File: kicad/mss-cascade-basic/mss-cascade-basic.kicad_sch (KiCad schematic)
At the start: 93 parts, among them J1 Screw_Terminal_01x02, J10 Screw_Terminal_01x02, J2 SM04B-SRSS, J3 SM04B-SRSS, J4 SM04B-SRSS, J5 8P8C, J6 8P8C, J7 AVR-ISP, J8 Screw_Terminal_01x02, J9 Screw_Terminal_01x02, U1 AP7381-50Y, U2 ATtiny861A-S, U3 74HC4049, U4 AP3012

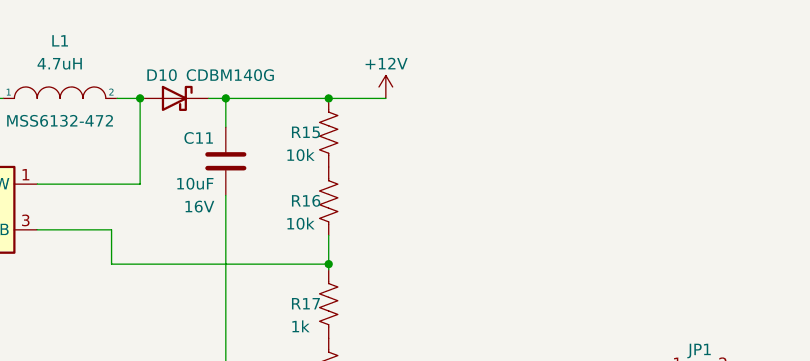
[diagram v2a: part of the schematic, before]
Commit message: Add test point for 12V, move connectors to align
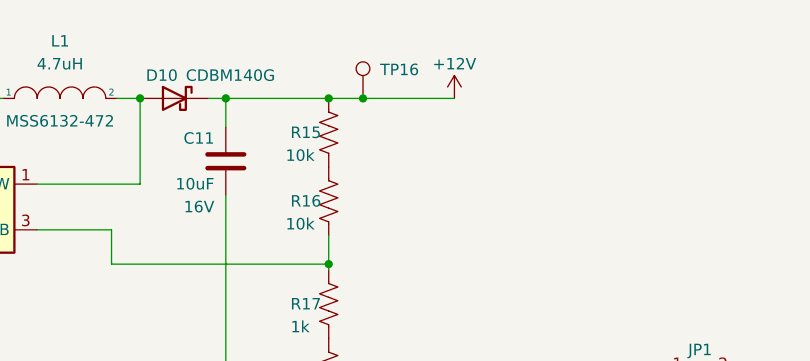
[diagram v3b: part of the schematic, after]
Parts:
- added TP16: TestPoint, TestPoint:TestPoint_Pad_D2.0mm, symbol Connector:TestPoint
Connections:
- net +12V: now also TP16.1
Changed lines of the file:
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@@
   (junction (at 121.92 64.77) (diameter 0) (color 0 0 0 0)
   )
+  (junction (at 198.12 22.86) (diameter 0) (color 0 0 0 0)
+  )
   (junction (at 244.475 70.485) (diameter 0) (color 0 0 0 0)
   )
@@
     (stroke (width 0) (type default) (color 0 0 0 0))
   )
-  (wire (pts (xy 194.31 22.86) (xy 200.66 22.86))
+  (wire (pts (xy 194.31 22.86) (xy 198.12 22.86))
     (stroke (width 0) (type default) (color 0 0 0 0))
   )
@@
     (stroke (width 0) (type default) (color 0 0 0 0))
   )
+  (wire (pts (xy 198.12 22.86) (xy 208.28 22.86))
+    (stroke (width 0) (type default) (color 0 0 0 0))
+  )
   (wire (pts (xy 119.38 120.65) (xy 121.92 120.65))
     (stroke (width 0) (type default) (color 0 0 0 0))
@@
     (pin "1")
   )
+  (symbol (lib_id "Connector:TestPoint") (at 198.12 22.86 0) (mirror y) (unit 1)
+    (in_bom yes) (on_board yes)
+    (property "Reference" "TP16" (id 0) (at 200.025 19.685 0)
+      (effects (font (size 1.27 1.27)) (justify right))
+    )
+    (property "Value" "TestPoint" (id 1) (at 196.215 20.8279 0)
+      (effects (font (size 1.27 1.27)) (justify left) hide)
+    )
+    (property "Footprint" "TestPoint:TestPoint_Pad_D2.0mm" (id 2) (at 193.04 22.86 0)
+      (effects (font (size 1.27 1.27)) hide)
+    )
+    (property "Datasheet" "~" (id 3) (at 193.04 22.86 0)
+      (effects (font (size 1.27 1.27)) hide)
+    )
+    (pin "1")
+  )
   (symbol (lib_id "Connector_Generic_MountingPin:Conn_01x04_MountingPin") (at 31.75 64.135 0) (mirror y) (unit 1)
     (in_bom yes) (on_board yes)
@@
     (pin "2")
   )
-  (symbol (lib_id "power:+12V") (at 200.66 22.86 0) (mirror y) (unit 1)
+  (symbol (lib_id "power:+12V") (at 208.28 22.86 0) (mirror y) (unit 1)
     (in_bom yes) (on_board yes)
-    (property "Reference" "#PWR022" (id 0) (at 200.66 26.67 0)
+    (property "Reference" "#PWR022" (id 0) (at 208.28 26.67 0)
       (effects (font (size 1.27 1.27)) hide)
     )
-    (property "Value" "+12V" (id 1) (at 200.66 19.05 0))
-    (property "Footprint" "" (id 2) (at 200.66 22.86 0)
+    (property "Value" "+12V" (id 1) (at 208.28 19.05 0))
+    (property "Footprint" "" (id 2) (at 208.28 22.86 0)
       (effects (font (size 1.27 1.27)) hide)
     )
-    (property "Datasheet" "" (id 3) (at 200.66 22.86 0)
+    (property "Datasheet" "" (id 3) (at 208.28 22.86 0)
       (effects (font (size 1.27 1.27)) hide)
     )
@@
       (reference "TP15") (unit 1) (value "TestPoint") (footprint "TestPoint:TestPoint_Pad_D2.0mm")
     )
+    (path "/0b9c37da-2612-485b-be8a-776d74b2a19d"
+      (reference "TP16") (unit 1) (value "TestPoint") (footprint "TestPoint:TestPoint_Pad_D2.0mm")
+    )
     (path "/7a02355a-c87d-4d7e-9caa-076f50357812"

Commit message: Update diode footprints on the cascade basic for proper SOD123T on all of the CDBM140Gs Update version to 1.1
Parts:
- D1, D10, D2, D3, D4, D7, D8: footprint Diode_SMD:D_SOD-123 -> ISE_Generic:SOD-123T
- U3: footprint (none) -> Package_SO:SO-16_3.9x9.9mm_P1.27mm
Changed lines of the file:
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@@
       (effects (font (size 1.27 1.27)) (justify right))
     )
-    (property "Footprint" "Diode_SMD:D_SOD-123" (id 2) (at 40.767 40.64 0)
+    (property "Footprint" "ISE_Generic:SOD-123T" (id 2) (at 40.767 40.64 0)
       (effects (font (size 1.27 1.27)) hide)
     )
@@
       (effects (font (size 1.27 1.27)) (justify right))
     )
-    (property "Footprint" "Diode_SMD:D_SOD-123" (id 2) (at 40.767 27.94 0)
+    (property "Footprint" "ISE_Generic:SOD-123T" (id 2) (at 40.767 27.94 0)
       (effects (font (size 1.27 1.27)) hide)
     )
@@
       (effects (font (size 1.27 1.27)) (justify left))
     )
-    (property "Footprint" "" (id 2) (at 185.42 169.545 0)
+    (property "Footprint" "Package_SO:SO-16_3.9x9.9mm_P1.27mm" (id 2) (at 185.42 169.545 0)
       (effects (font (size 1.27 1.27)) hide)
     )
@@
       (effects (font (size 1.27 1.27)) (justify right))
     )
-    (property "Footprint" "Diode_SMD:D_SOD-123" (id 2) (at 40.767 35.56 0)
+    (property "Footprint" "ISE_Generic:SOD-123T" (id 2) (at 40.767 35.56 0)
       (effects (font (size 1.27 1.27)) hide)
     )
@@
     (property "Reference" "U3" (id 0) (at 142.875 182.88 0))
     (property "Value" "74HC4049" (id 1) (at 146.05 189.23 0))
-    (property "Footprint" "" (id 2) (at 140.335 186.055 0)
+    (property "Footprint" "Package_SO:SO-16_3.9x9.9mm_P1.27mm" (id 2) (at 140.335 186.055 0)
       (effects (font (size 1.27 1.27)) hide)
     )
@@
     (property "Reference" "U3" (id 0) (at 143.51 129.54 0))
     (property "Value" "74HC4049" (id 1) (at 146.685 135.89 0))
-    (property "Footprint" "" (id 2) (at 140.335 132.715 0)
+    (property "Footprint" "Package_SO:SO-16_3.9x9.9mm_P1.27mm" (id 2) (at 140.335 132.715 0)
       (effects (font (size 1.27 1.27)) hide)
     )
@@
     (property "Reference" "U3" (id 0) (at 144.145 140.97 0))
     (property "Value" "74HC4049" (id 1) (at 146.685 146.685 0))
-    (property "Footprint" "" (id 2) (at 140.335 143.51 0)
+    (property "Footprint" "Package_SO:SO-16_3.9x9.9mm_P1.27mm" (id 2) (at 140.335 143.51 0)
       (effects (font (size 1.27 1.27)) hide)
     )
@@
       (effects (font (size 1.27 1.27)) (justify right))
     )
-    (property "Footprint" "Diode_SMD:D_SOD-123" (id 2) (at 54.61 73.66 0)
+    (property "Footprint" "ISE_Generic:SOD-123T" (id 2) (at 54.61 73.66 0)
       (effects (font (size 1.27 1.27)) hide)
     )
@@
       (effects (font (size 1.27 1.27)) (justify right))
     )
-    (property "Footprint" "Diode_SMD:D_SOD-123" (id 2) (at 177.165 22.86 0)
+    (property "Footprint" "ISE_Generic:SOD-123T" (id 2) (at 177.165 22.86 0)
       (effects (font (size 1.27 1.27)) hide)
     )
@@
     (property "Reference" "U3" (id 0) (at 142.875 161.925 0))
     (property "Value" "74HC4049" (id 1) (at 146.05 168.275 0))
-    (property "Footprint" "" (id 2) (at 140.335 165.1 0)
+    (property "Footprint" "Package_SO:SO-16_3.9x9.9mm_P1.27mm" (id 2) (at 140.335 165.1 0)
       (effects (font (size 1.27 1.27)) hide)
     )
@@
       (effects (font (size 1.27 1.27)) (justify right))
     )
-    (property "Footprint" "Diode_SMD:D_SOD-123" (id 2) (at 57.15 66.675 0)
+    (property "Footprint" "ISE_Generic:SOD-123T" (id 2) (at 57.15 66.675 0)
       (effects (font (size 1.27 1.27)) hide)
     )
@@
       (effects (font (size 1.27 1.27)) (justify right))
     )
-    (property "Footprint" "Diode_SMD:D_SOD-123" (id 2) (at 40.767 22.86 0)
+    (property "Footprint" "ISE_Generic:SOD-123T" (id 2) (at 40.767 22.86 0)
       (effects (font (size 1.27 1.27)) hide)
     )
@@
     (property "Reference" "U3" (id 0) (at 142.875 172.085 0))
     (property "Value" "74HC4049" (id 1) (at 146.05 178.435 0))
-    (property "Footprint" "" (id 2) (at 140.335 175.26 0)
+    (property "Footprint" "Package_SO:SO-16_3.9x9.9mm_P1.27mm" (id 2) (at 140.335 175.26 0)
       (effects (font (size 1.27 1.27)) hide)
     )
@@
     (property "Reference" "U3" (id 0) (at 142.875 151.13 0))
     (property "Value" "74HC4049" (id 1) (at 146.05 157.48 0))
-    (property "Footprint" "" (id 2) (at 140.335 154.305 0)
+    (property "Footprint" "Package_SO:SO-16_3.9x9.9mm_P1.27mm" (id 2) (at 140.335 154.305 0)
       (effects (font (size 1.27 1.27)) hide)
     )
@@
     )
     (path "/a444bcfb-6fe3-4163-8bfb-714876967d65"
-      (reference "D1") (unit 1) (value "CDBM140G") (footprint "Diode_SMD:D_SOD-123")
+      (reference "D1") (unit 1) (value "CDBM140G") (footprint "ISE_Generic:SOD-123T")
     )
     (path "/233fd880-ea9b-4abb-a894-7ec6225937a5"
-      (reference "D2") (unit 1) (value "CDBM140G") (footprint "Diode_SMD:D_SOD-123")
+      (reference "D2") (unit 1) (value "CDBM140G") (footprint "ISE_Generic:SOD-123T")
     )
     (path "/272b5079-febe-45c0-afce-93f155af0579"
-      (reference "D3") (unit 1) (value "CDBM140G") (footprint "Diode_SMD:D_SOD-123")
+      (reference "D3") (unit 1) (value "CDBM140G") (footprint "ISE_Generic:SOD-123T")
     )
     (path "/0fe61260-85d0-4e22-afc7-ca87aa02fb0c"
-      (reference "D4") (unit 1) (value "CDBM140G") (footprint "Diode_SMD:D_SOD-123")
+      (reference "D4") (unit 1) (value "CDBM140G") (footprint "ISE_Generic:SOD-123T")
     )
     (path "/22f47f5e-ca58-41d5-9733-099d3d864c0b"
@@
     )
     (path "/6214705d-b9f1-48f8-be44-36702cad6cb2"
-      (reference "D7") (unit 1) (value "CDBM140G") (footprint "Diode_SMD:D_SOD-123")
+      (reference "D7") (unit 1) (value "CDBM140G") (footprint "ISE_Generic:SOD-123T")
     )
     (path "/9add5774-648f-4cbe-9e4c-f503651f61c3"
-      (reference "D8") (unit 1) (value "CDBM140G") (footprint "Diode_SMD:D_SOD-123")
+      (reference "D8") (unit 1) (value "CDBM140G") (footprint "ISE_Generic:SOD-123T")
     )
     (path "/1e9c982d-7f4d-4846-9d0f-7887e9be83e2"
@@
     )
     (path "/83515395-b131-4066-8f71-ee5847f90081"
-      (reference "D10") (unit 1) (value "CDBM140G") (footprint "Diode_SMD:D_SOD-123")
+      (reference "D10") (unit 1) (value "CDBM140G") (footprint "ISE_Generic:SOD-123T")
     )
     (path "/fedd826e-74ae-4512-8096-f38aaffedb7c"
@@
     )
     (path "/4db4acf3-3390-438b-9512-752428aff293"
-      (reference "U3") (unit 1) (value "74HC4049") (footprint "")
+      (reference "U3") (unit 1) (value "74HC4049") (footprint "Package_SO:SO-16_3.9x9.9mm_P1.27mm")
     )
     (path "/5942d4ea-a573-402c-b724-a6ea9aa0b3a5"
-      (reference "U3") (unit 2) (value "74HC4049") (footprint "")
+      (reference "U3") (unit 2) (value "74HC4049") (footprint "Package_SO:SO-16_3.9x9.9mm_P1.27mm")
     )
     (path "/fa95d9cf-d026-48b0-9146-91424f176256"
-      (reference "U3") (unit 3) (value "74HC4049") (footprint "")
+      (reference "U3") (unit 3) (value "74HC4049") (footprint "Package_SO:SO-16_3.9x9.9mm_P1.27mm")
     )
     (path "/31f0d2b3-2f1a-4b7c-be1d-508f567b17b7"
-      (reference "U3") (unit 4) (value "74HC4049") (footprint "")
+      (reference "U3") (unit 4) (value "74HC4049") (footprint "Package_SO:SO-16_3.9x9.9mm_P1.27mm")
     )
     (path "/c64a0ca9-d689-4da1-bc57-59534c75b71a"
-      (reference "U3") (unit 5) (value "74HC4049") (footprint "")
+      (reference "U3") (unit 5) (value "74HC4049") (footprint "Package_SO:SO-16_3.9x9.9mm_P1.27mm")
     )
     (path "/973f1b88-f1a2-4172-95f3-92ec4f77b1a5"
-      (reference "U3") (unit 6) (value "74HC4049") (footprint "")
+      (reference "U3") (unit 6) (value "74HC4049") (footprint "Package_SO:SO-16_3.9x9.9mm_P1.27mm")
     )
     (path "/24be55f7-7315-498d-a33e-4bf390f726f9"
-      (reference "U3") (unit 7) (value "74HC4049") (footprint "")
+      (reference "U3") (unit 7) (value "74HC4049") (footprint "Package_SO:SO-16_3.9x9.9mm_P1.27mm")
     )
     (path "/a3a6f801-6db5-46a8-b468-ee8eabdc30e8"
